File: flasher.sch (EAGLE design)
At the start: 37 parts, among them IC2 TINY85-20-DIP, Q1 2N2222, U1 CL2N3, U2 CL2N3, U3 CL2N3, U4 CL2N3, U5 CL2N3, U6 CL2N3

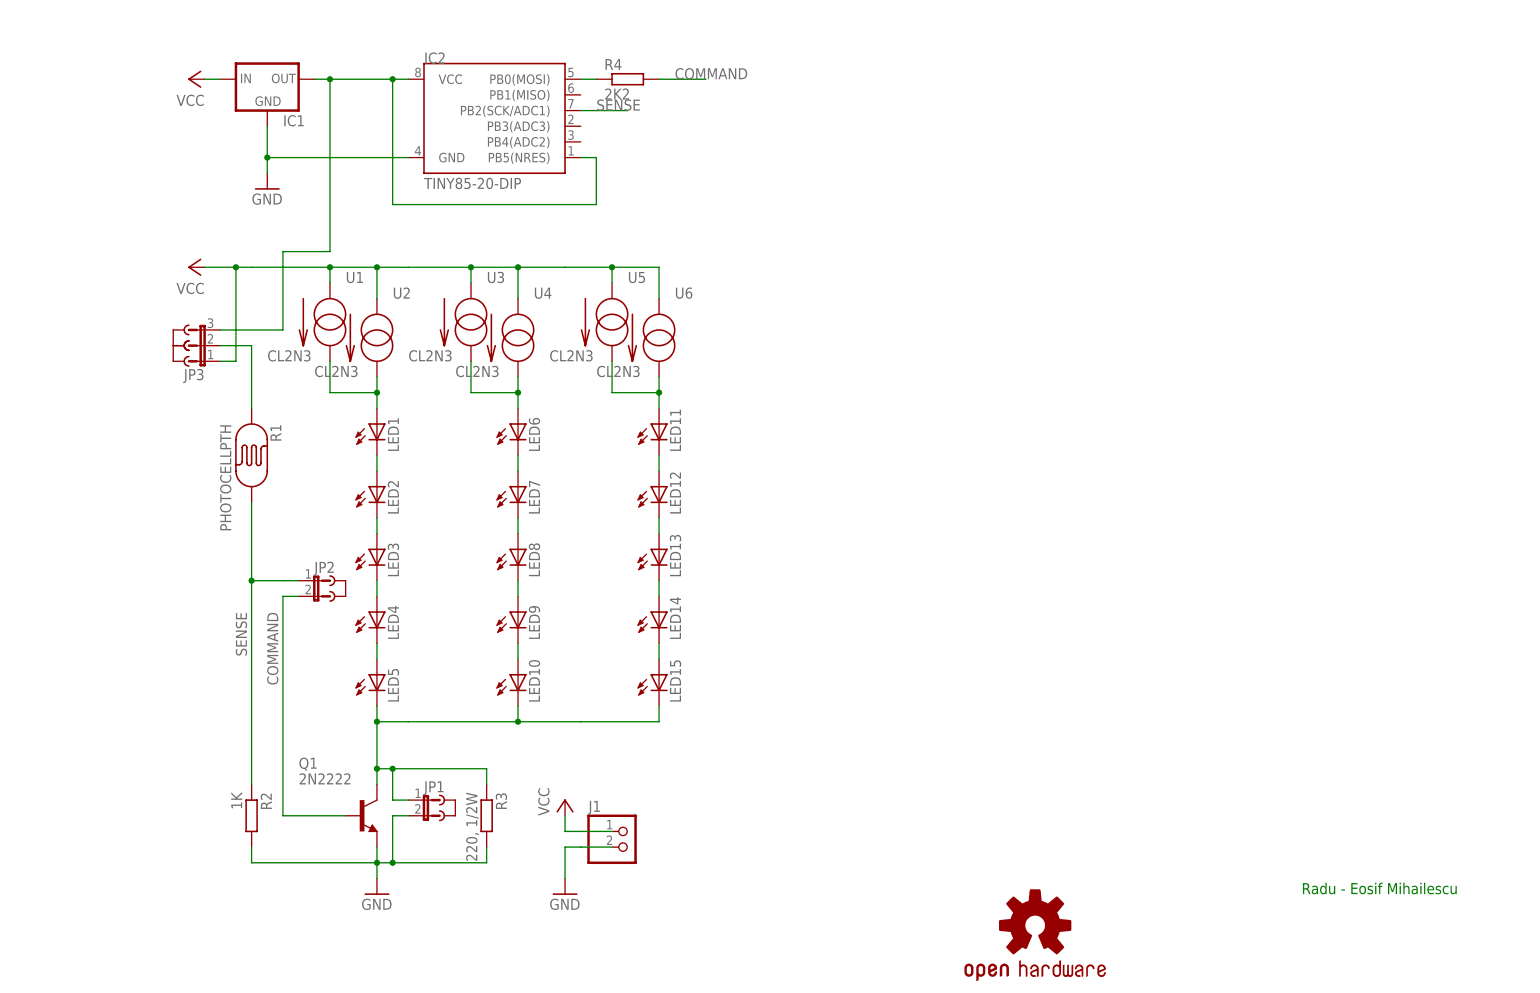
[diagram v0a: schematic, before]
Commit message: Final version, so far - brought flasher to ready for manufacture - done away with Pro assembly variant, not feasible - made design more robust, doing away with power resistor - sorted top silk, added branding and extra artwork - made flip-compatible (can be assembled as left or right hand side using same PCB)
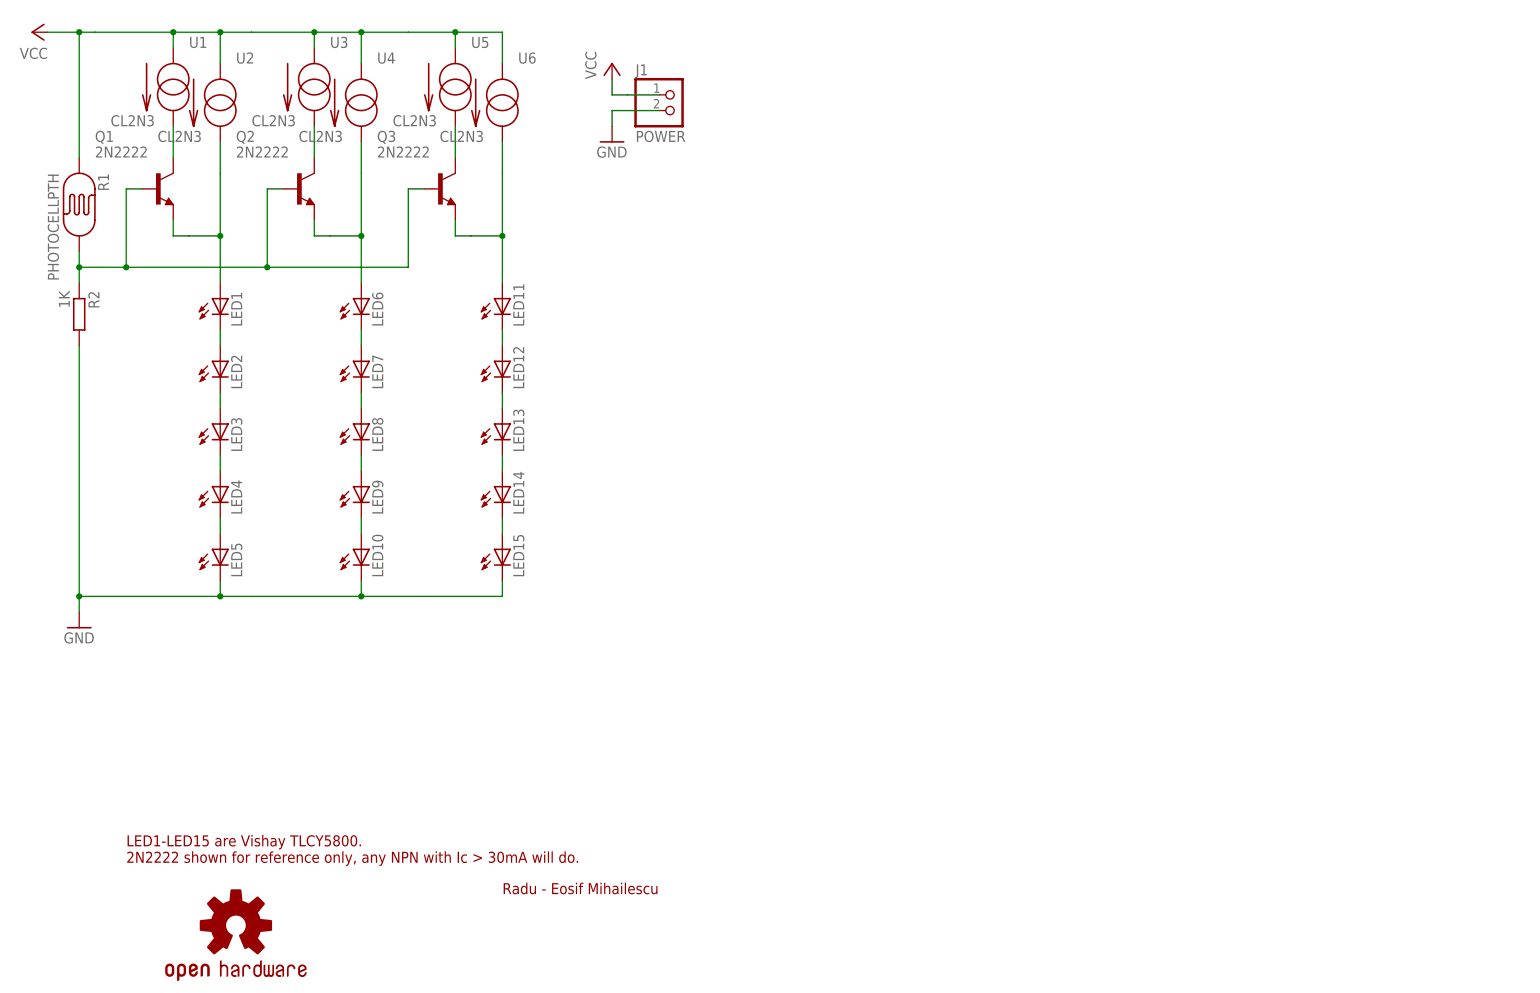
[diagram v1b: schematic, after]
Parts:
- removed IC1: (no value), SparkFun-PowerIC:V_REG_78XXTO-92
- removed IC2: TINY85-20-DIP, SparkFun-DigitalIC:ATTINY45TINY85-20-DIP
- removed JP1, JP2: (no value), jumper:JP1E
- removed JP1C, JP2C, JP3C1, JP3C2: (no value), jumper:JUMPER
- removed JP3: (no value), jumper:JP2E
- removed R3: 220, 1/2W, rcl:R-EU_0204/7
- removed R4: 2K2, rcl:R-EU_0204/7
- added Q2, Q3: 2N2222, transistor-neu-to92:2N2222-NPN-TO92-EBC
- J1: value (none) -> POWER
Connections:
- removed net COMMAND: JP2.2, Q1.B, R4.2
- removed net N$19: JP1.1, LED10.C, LED15.C, LED5.C, Q1.C, R3.1
- net GND: now also LED10.C, LED15.C, LED5.C; no longer IC1.GND, IC2.GND, JP1.2, Q1.E, R3.2
- net N$11: now also Q2.E; no longer U3.OUT
- net N$13: now also Q3.C, U5.OUT; no longer JP3.2, R1.P$1
- net N$17: now also Q3.E; no longer U5.OUT
- net N$4: now also Q1.E; no longer U1.OUT
- net N$6: now also Q1.C, U1.OUT; no longer IC2.PB0(MOSI), R4.1
- net N$7: now also Q2.C, U3.OUT; no longer IC1.OUT, IC2.PB5(NRES), IC2.VCC, JP3.3
- net SENSE: now also Q1.B, Q2.B, Q3.B; no longer IC2.PB2(SCK/ADC1), JP2.1
- net VCC: now also R1.P$1; no longer IC1.IN, JP3.1
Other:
- note added: "LED1-LED15 are Vishay TLCY5800. 2N2222 shown for reference only, any NPN with Ic > 30mA will do."
- moved on the sheet: J1, LED1, LED10, LED11, LED12, LED13, LED14, LED15, LED2, LED3, LED4, LED5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

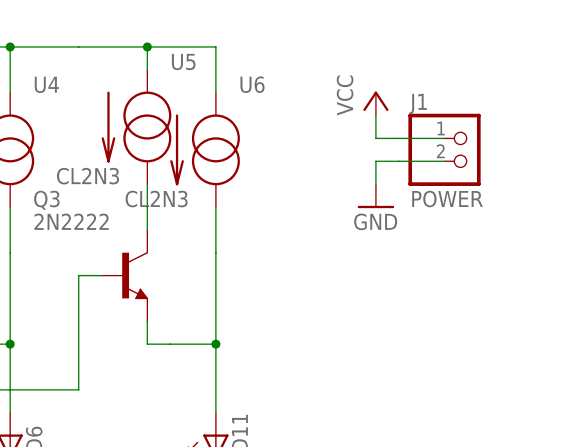
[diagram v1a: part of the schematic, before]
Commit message: BUGFIX: - added 0.1uF as recommended by Supertex CL2N3 datasheet - rotated power connector to make it more accessible during assembly
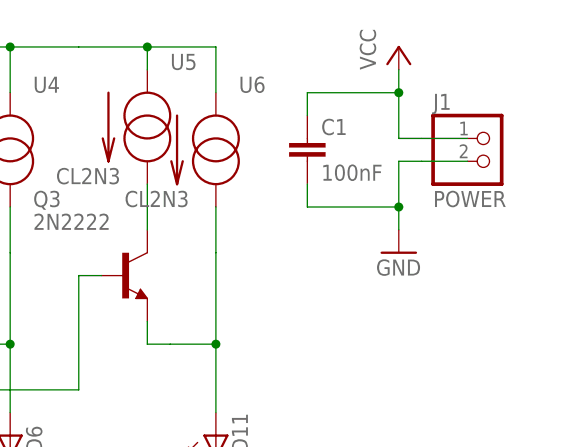
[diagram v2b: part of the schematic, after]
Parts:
- added C1: 100nF, rcl:C-EU050-025X075
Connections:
- net GND: now also C1.2
- net VCC: now also C1.1
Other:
- moved on the sheet: J1
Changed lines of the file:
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@@
 </part>
 <part name="FRAME2" library="frames" deviceset="A5P-LOC" device=""/>
+<part name="C1" library="rcl" deviceset="C-EU" device="050-025X075" value="100nF"/>
 </parts>
 <sheets>
@@
 <instance part="U1" gate="G$1" x="35.56" y="149.86"/>
 <instance part="U2" gate="G$1" x="43.18" y="147.32"/>
-<instance part="P+2" gate="VCC" x="106.68" y="154.94"/>
-<instance part="GND2" gate="1" x="106.68" y="142.24"/>
+<instance part="P+2" gate="VCC" x="109.22" y="160.02"/>
+<instance part="GND2" gate="1" x="109.22" y="137.16"/>
 <instance part="LED6" gate="G$1" x="66.04" y="116.84"/>
 <instance part="LED7" gate="G$1" x="66.04" y="106.68"/>
@@
 <instance part="U6" gate="G$1" x="88.9" y="147.32"/>
 <instance part="LOGO1" gate="G$1" x="45.72" y="15.24"/>
-<instance part="J1" gate="G$1" x="116.84" y="147.32"/>
+<instance part="J1" gate="G$1" x="119.38" y="147.32"/>
 <instance part="Q2" gate="G$1" x="55.88" y="134.62"/>
 <instance part="Q3" gate="G$1" x="78.74" y="134.62"/>
 <instance part="FRAME2" gate="G$1" x="0" y="0"/>
+<instance part="C1" gate="G$1" x="99.06" y="149.86"/>
 </instances>
 <busses>
@@
 <segment>
 <pinref part="GND2" gate="1" pin="GND"/>
-<wire x1="109.22" y1="147.32" x2="106.68" y2="147.32" width="0.1524" layer="91"/>
-<wire x1="106.68" y1="147.32" x2="106.68" y2="144.78" width="0.1524" layer="91"/>
+<wire x1="111.76" y1="147.32" x2="109.22" y2="147.32" width="0.1524" layer="91"/>
+<wire x1="109.22" y1="147.32" x2="109.22" y2="142.24" width="0.1524" layer="91"/>
 <pinref part="J1" gate="G$1" pin="2"/>
-<wire x1="109.22" y1="147.32" x2="114.3" y2="147.32" width="0.1524" layer="91"/>
+<wire x1="109.22" y1="142.24" x2="109.22" y2="139.7" width="0.1524" layer="91"/>
+<wire x1="111.76" y1="147.32" x2="116.84" y2="147.32" width="0.1524" layer="91"/>
+<pinref part="C1" gate="G$1" pin="2"/>
+<wire x1="99.06" y1="144.78" x2="99.06" y2="142.24" width="0.1524" layer="91"/>
+<wire x1="99.06" y1="142.24" x2="109.22" y2="142.24" width="0.1524" layer="91"/>
+<junction x="109.22" y="142.24"/>
 </segment>
 <segment>
@@
 <segment>
 <pinref part="P+2" gate="VCC" pin="VCC"/>
-<wire x1="106.68" y1="152.4" x2="106.68" y2="149.86" width="0.1524" layer="91"/>
-<wire x1="106.68" y1="149.86" x2="109.22" y2="149.86" width="0.1524" layer="91"/>
+<wire x1="109.22" y1="157.48" x2="109.22" y2="154.94" width="0.1524" layer="91"/>
+<wire x1="109.22" y1="154.94" x2="109.22" y2="149.86" width="0.1524" layer="91"/>
+<wire x1="109.22" y1="149.86" x2="111.76" y2="149.86" width="0.1524" layer="91"/>
 <pinref part="J1" gate="G$1" pin="1"/>
-<wire x1="109.22" y1="149.86" x2="114.3" y2="149.86" width="0.1524" layer="91"/>
+<wire x1="111.76" y1="149.86" x2="116.84" y2="149.86" width="0.1524" layer="91"/>
+<pinref part="C1" gate="G$1" pin="1"/>
+<wire x1="99.06" y1="152.4" x2="99.06" y2="154.94" width="0.1524" layer="91"/>
+<wire x1="99.06" y1="154.94" x2="109.22" y2="154.94" width="0.1524" layer="91"/>
+<junction x="109.22" y="154.94"/>
 </segment>
 </net>
